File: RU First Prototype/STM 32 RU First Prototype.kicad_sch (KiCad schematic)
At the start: 79 parts, among them J1 Conn_01x02, J10 Conn_01x02, J2 USB_C_Receptacle, J3 Conn_01x02, J4 Conn_01x04, J5 Screw_Terminal, J6 Screw_Terminal, J7 Screw_Terminal, J8 Screw_Terminal, J9 Screw_Terminal, Q1 NMOS, Q1 SISA96DN-T1, Q2 SISA96DN-T1, Q3 SISA96DN-T1, Q4 SISA96DN-T1, SW1 SW_SPDT, U1 STM32F412RGTx, U2 AMS1117-3.3, U3 MS5611, U4 KX134-1211, U5 W25Q16JVSS, U6 TCAN330, U7 TCAN330, Y1 Crystal_25Mhz

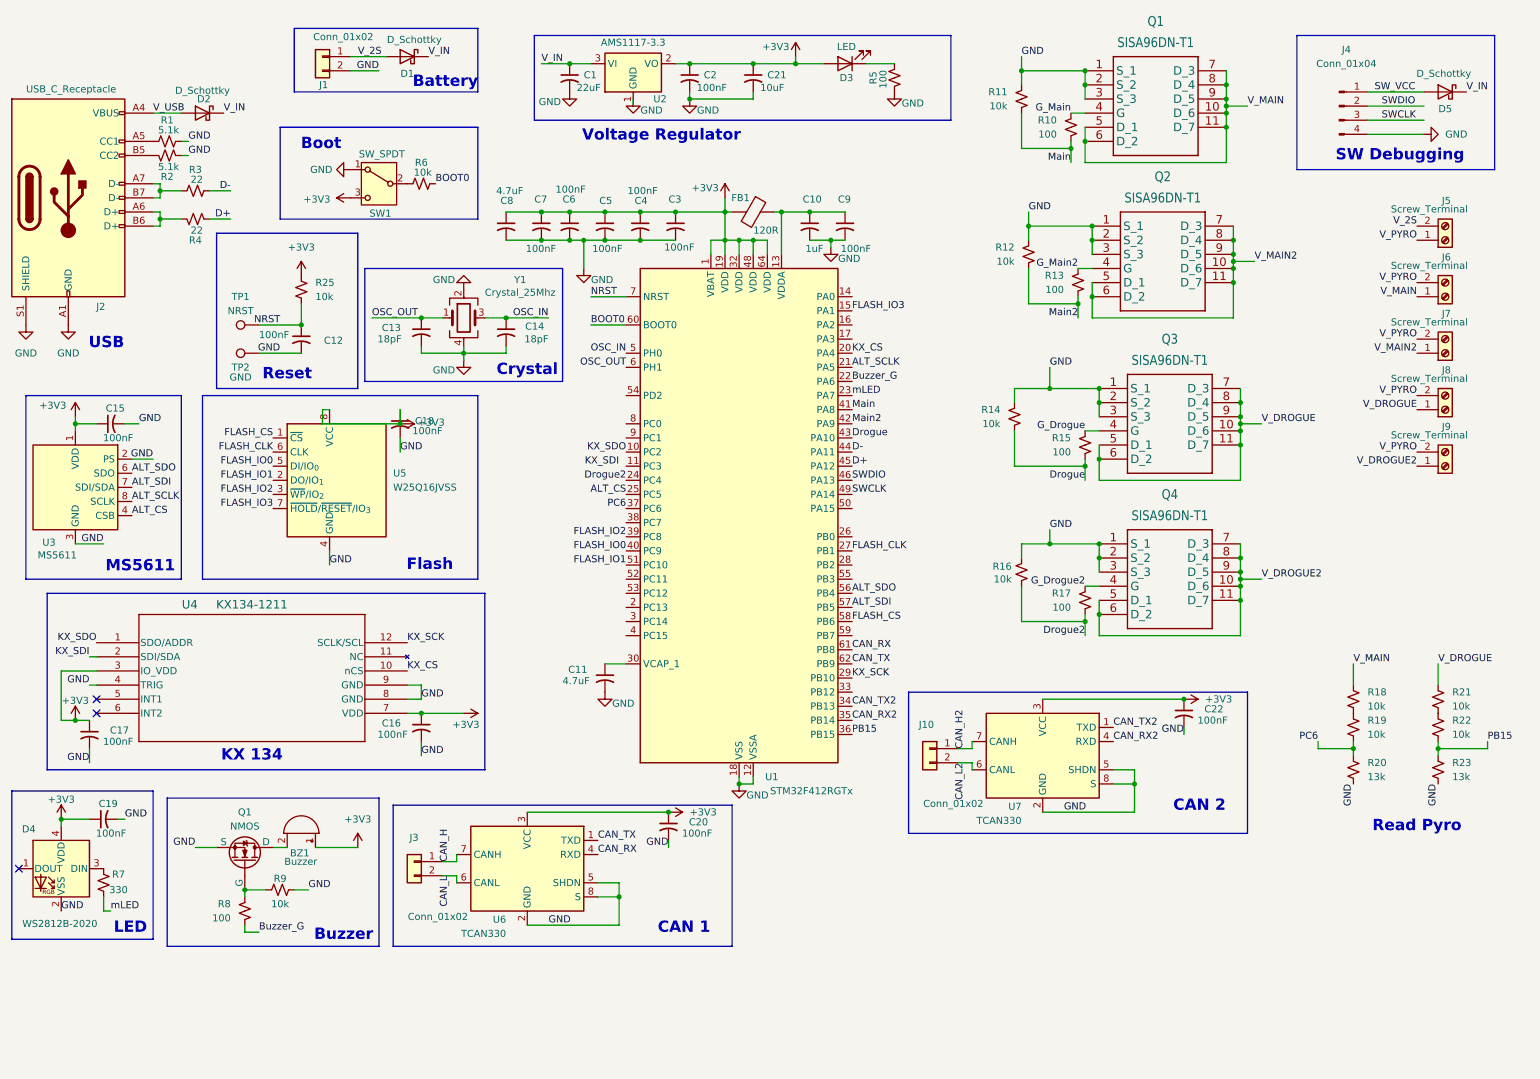
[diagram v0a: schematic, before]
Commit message: Schematic adjusted for symbols and footprint assignments, and I2C replaced with SPI
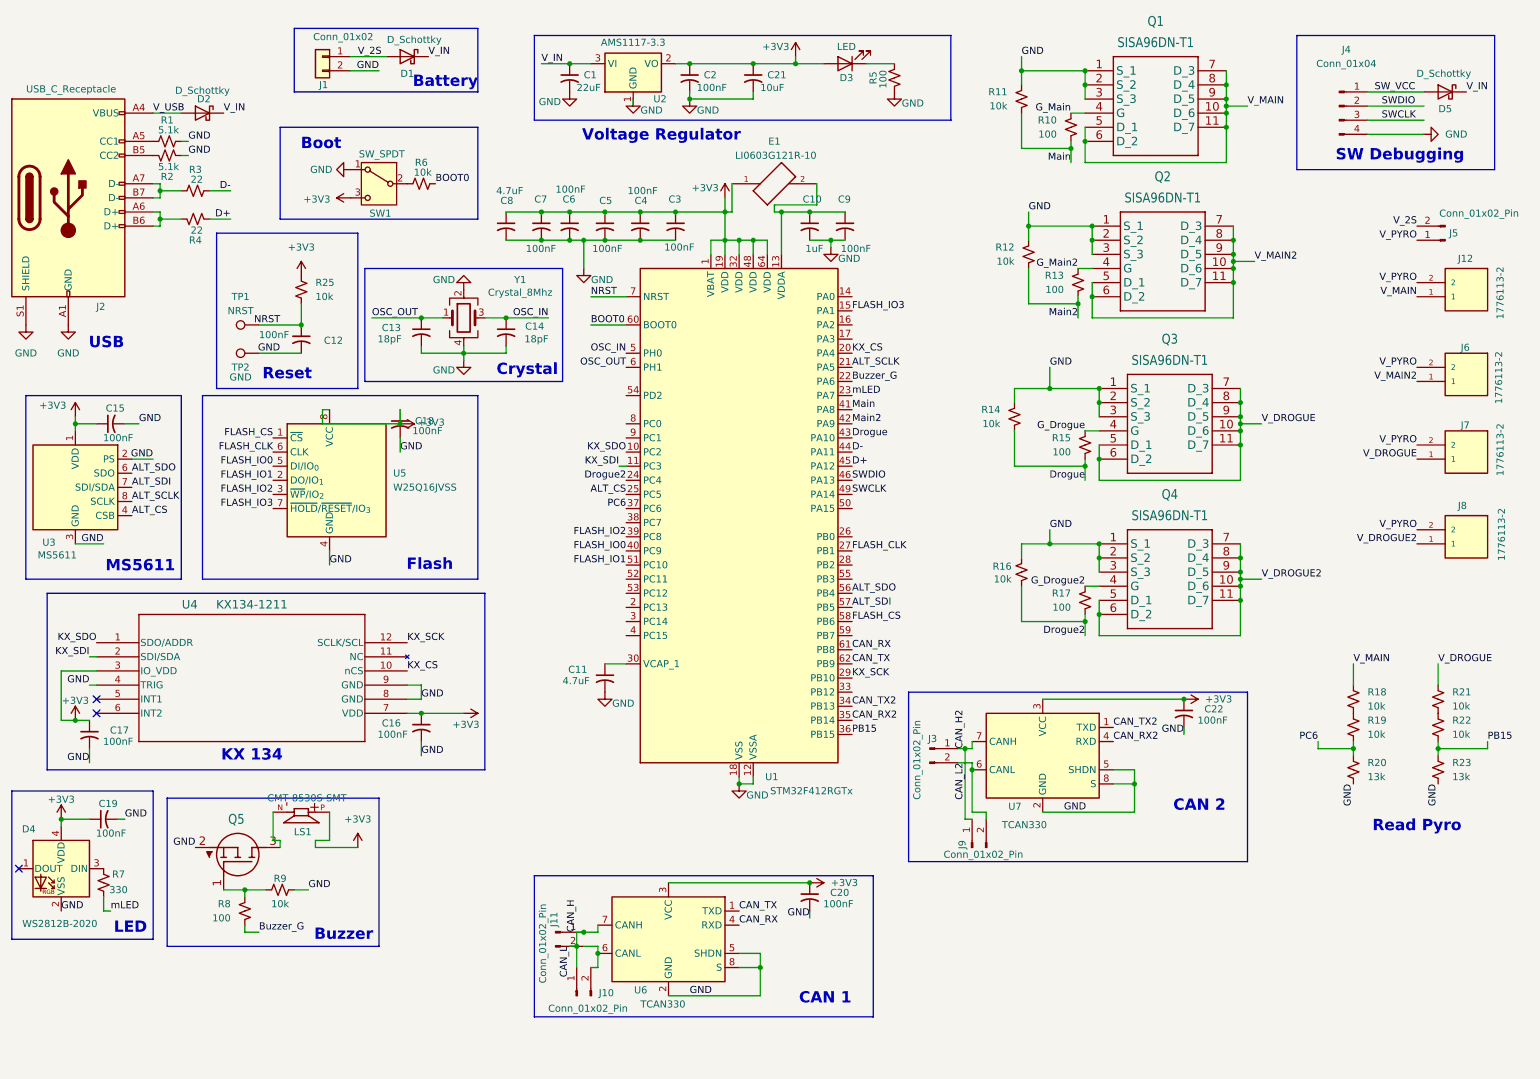
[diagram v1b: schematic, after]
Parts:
- removed BZ1: Buzzer, symbol Device:Buzzer
- removed FB1: 120R, symbol Device:FerriteBead
- removed J10, J3: Conn_01x02, Connector_AMASS:AMASS_XT30PW-F_1x02_P2.50mm_Horizontal, symbol Connector_Generic:Conn_01x02
- removed J5, J6, J7, J8, J9: Screw_Terminal, symbol Connector:Screw_Terminal_01x02
- removed Q1: NMOS, symbol Simulation_SPICE:NMOS
- added E1: LI0603G121R-10, LI0603G121R-10:FB_LI0603G121R-10, symbol LI0603G121R-10:LI0603G121R-10
- added J10, J11, J3, J5, J9: Conn_01x02_Pin, Connector_AMASS:AMASS_XT30PW-M_1x02_P2.50mm_Horizontal, symbol Connector:Conn_01x02_Pin
- added J12, J6, J7, J8: 1776113-2, 1776113-2:TE_1776113-2, symbol 1776113-2:1776113-2
- added LS1: CMT-8530S-SMT, CMT-8530S-SMT:CUI_CMT-8530S-SMT, symbol CMT-8530S-SMT:CMT-8530S-SMT
- added Q5: ~, CJ3400:SOT95P240X115-3N, symbol CJ3400:CJ3400
- Y1: value Crystal_25Mhz -> Crystal_8Mhz
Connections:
- net CAN_L2 is gone; now on net CAN_H2: U7.6 (CANL)
- net +3V3: now also E1.1, LS1.P
- net CAN_H: now also J10.1 (Pin_1), J11.1 (Pin_1)
- net CAN_H2: now also J3.1 (Pin_1), J3.2 (Pin_2), J9.1 (Pin_1), J9.2 (Pin_2)
- net GND: now also Q5.2 (S)
- net KX_SDI: now also U1.11 (PC3)
- net V_2S: now also J5.2 (Pin_2)
- net V_DROGUE: now also J7.1
- net V_DROGUE2: now also J8.1
- net V_MAIN: now also J12.1
- net V_MAIN2: now also J6.1
- net V_PYRO: now also J12.2, J5.1 (Pin_1), J6.2, J7.2, J8.2
- net at R8.1, R9.2: now also Q5.1 (G)
- net at C10.1, C9.1, U1.13 (VDDA): now also E1.2
- net CAN_L: no longer names the net of U6.6 (CANL)
- net CAN_L: now also J10.2 (Pin_2), J11.2 (Pin_2)
- new net: LS1.N, Q5.3 (D)
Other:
- moved on the sheet: C20, U6

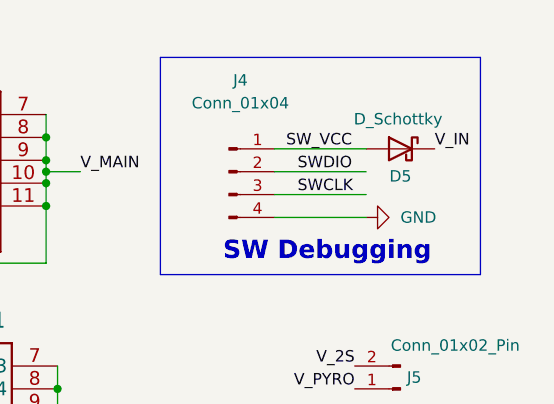
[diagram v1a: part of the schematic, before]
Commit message: Added missing footprints
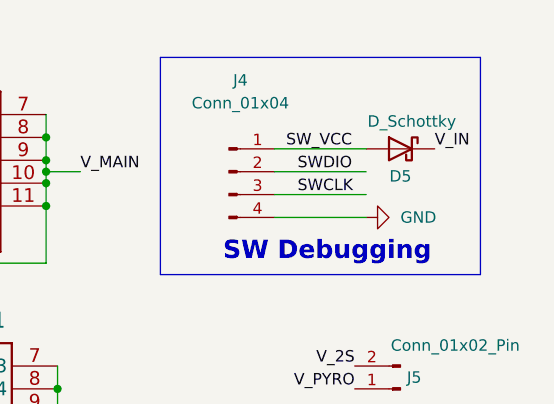
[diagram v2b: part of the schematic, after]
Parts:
- D1, D2, D5: footprint (none) -> Diode_SMD:D_SOD-128
- D3: footprint (none) -> Diode_SMD:D_0603_1608Metric
- Q1, Q2, Q3, Q4: footprint SISA96DN-T1-GE3:SIS862DNT1GE3 -> SISA96DN-T1:SIS862DNT1GE3
- U4: footprint LGA12_2X2X0P9_ROM -> KX134-1211:XDCR_KX003-1077
- Y1: footprint (none) -> Crystal:Crystal_SMD_7050-4Pin_7.0x5.0mm
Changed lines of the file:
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@@
 			)
 		)
-		(property "Footprint" "SISA96DN-T1-GE3:SIS862DNT1GE3"
+		(property "Footprint" "SISA96DN-T1:SIS862DNT1GE3"
 			(at 208.28 50.8 0)
 			(effects
@@
 			)
 		)
-		(property "Footprint" "SISA96DN-T1-GE3:SIS862DNT1GE3"
+		(property "Footprint" "SISA96DN-T1:SIS862DNT1GE3"
 			(at 209.55 80.01 0)
 			(effects
@@
 	)
 	(symbol
+		(lib_id "Device:D_Schottky")
+		(at 271.78 26.67 0)
+		(mirror y)
+		(unit 1)
+		(exclude_from_sim no)
+		(in_bom yes)
+		(on_board yes)
+		(dnp no)
+		(property "Reference" "D5"
+			(at 271.78 29.718 0)
+			(effects
+				(font
+					(size 1.27 1.27)
+				)
+			)
+		)
+		(property "Value" "D_Schottky"
+			(at 273.05 23.622 0)
+			(effects
+				(font
+					(size 1.27 1.27)
+				)
+			)
+		)
+		(property "Footprint" "Diode_SMD:D_SOD-128"
+			(at 271.78 26.67 0)
+			(effects
+				(font
+					(size 1.27 1.27)
+				)
+				(hide yes)
+			)
+		)
+		(property "Datasheet" "~"
+			(at 271.78 26.67 0)
+			(effects
+				(font
+					(size 1.27 1.27)
+				)
+				(hide yes)
+			)
+		)
+		(property "Description" "Schottky diode"
+			(at 271.78 26.67 0)
+			(effects
+				(font
+					(size 1.27 1.27)
+				)
+				(hide yes)
+			)
+		)
+		(pin "2"
+		)
+		(pin "1"
+		)
+		(instances
+			(project "STM 32 RU First Prototype"
+				(path "/73d1f315-8edb-4411-831f-b26c874dd7b7"
+					(reference "D5")
+					(unit 1)
+				)
+			)
+		)
+	)
+	(symbol
 		(lib_id "Device:C_Small_US")
 		(at 109.22 50.8 0)
@@
 			)
 		)
-		(property "Footprint" ""
+		(property "Footprint" "Diode_SMD:D_0603_1608Metric"
 			(at 163.83 21.59 0)
 			(effects
@@
 	)
 	(symbol
-		(lib_id "Device:D_Schottky")
-		(at 271.78 26.67 0)
-		(mirror y)
-		(unit 1)
-		(exclude_from_sim no)
-		(in_bom yes)
-		(on_board yes)
-		(dnp no)
-		(property "Reference" "D5"
-			(at 271.78 29.718 0)
-			(effects
-				(font
-					(size 1.27 1.27)
-				)
-			)
-		)
-		(property "Value" "D_Schottky"
-			(at 271.526 23.368 0)
-			(effects
-				(font
-					(size 1.27 1.27)
-				)
-			)
-		)
-		(property "Footprint" ""
-			(at 271.78 26.67 0)
-			(effects
-				(font
-					(size 1.27 1.27)
-				)
-				(hide yes)
-			)
-		)
-		(property "Datasheet" ""
-			(at 271.78 26.67 0)
-			(effects
-				(font
-					(size 1.27 1.27)
-				)
-				(hide yes)
-			)
-		)
-		(property "Description" "Schottky diode"
-			(at 271.78 26.67 0)
-			(effects
-				(font
-					(size 1.27 1.27)
-				)
-				(hide yes)
-			)
-		)
-		(pin "2"
-		)
-		(pin "1"
-		)
-		(instances
-			(project "STM 32 RU First Prototype"
-				(path "/73d1f315-8edb-4411-831f-b26c874dd7b7"
-					(reference "D5")
-					(unit 1)
-				)
-			)
-		)
-	)
-	(symbol
 		(lib_id "Device:C_Small_US")
 		(at 30.48 157.48 90)
@@
 			)
 		)
-		(property "Footprint" "SISA96DN-T1-GE3:SIS862DNT1GE3"
+		(property "Footprint" "SISA96DN-T1:SIS862DNT1GE3"
 			(at 207.01 22.86 0)
 			(effects
@@
 			)
 		)
-		(property "Footprint" "SISA96DN-T1-GE3:SIS862DNT1GE3"
+		(property "Footprint" "SISA96DN-T1:SIS862DNT1GE3"
 			(at 209.55 107.95 0)
 			(effects
@@
 			)
 		)
-		(property "Footprint" ""
+		(property "Footprint" "Crystal:Crystal_SMD_7050-4Pin_7.0x5.0mm"
 			(at 95.25 67.31 0)
 			(effects
@@
 			)
 		)
-		(property "Footprint" ""
+		(property "Footprint" "Diode_SMD:D_SOD-128"
 			(at 85.09 20.32 0)
 			(effects
@@
 			)
 		)
-		(property "Datasheet" ""
+		(property "Datasheet" "~"
 			(at 85.09 20.32 0)
 			(effects
@@
 			)
 		)
-		(property "Footprint" "LGA12_2X2X0P9_ROM"
+		(property "Footprint" "KX134-1211:XDCR_KX003-1077"
 			(at 29.21 125.73 0)
 			(effects
@@
 			)
 		)
-		(property "Footprint" ""
+		(property "Footprint" "Diode_SMD:D_SOD-128"
 			(at 48.26 30.48 0)
 			(effects
@@
 			)
 		)
-		(property "Datasheet" ""
+		(property "Datasheet" "~"
 			(at 48.26 30.48 0)
 			(effects

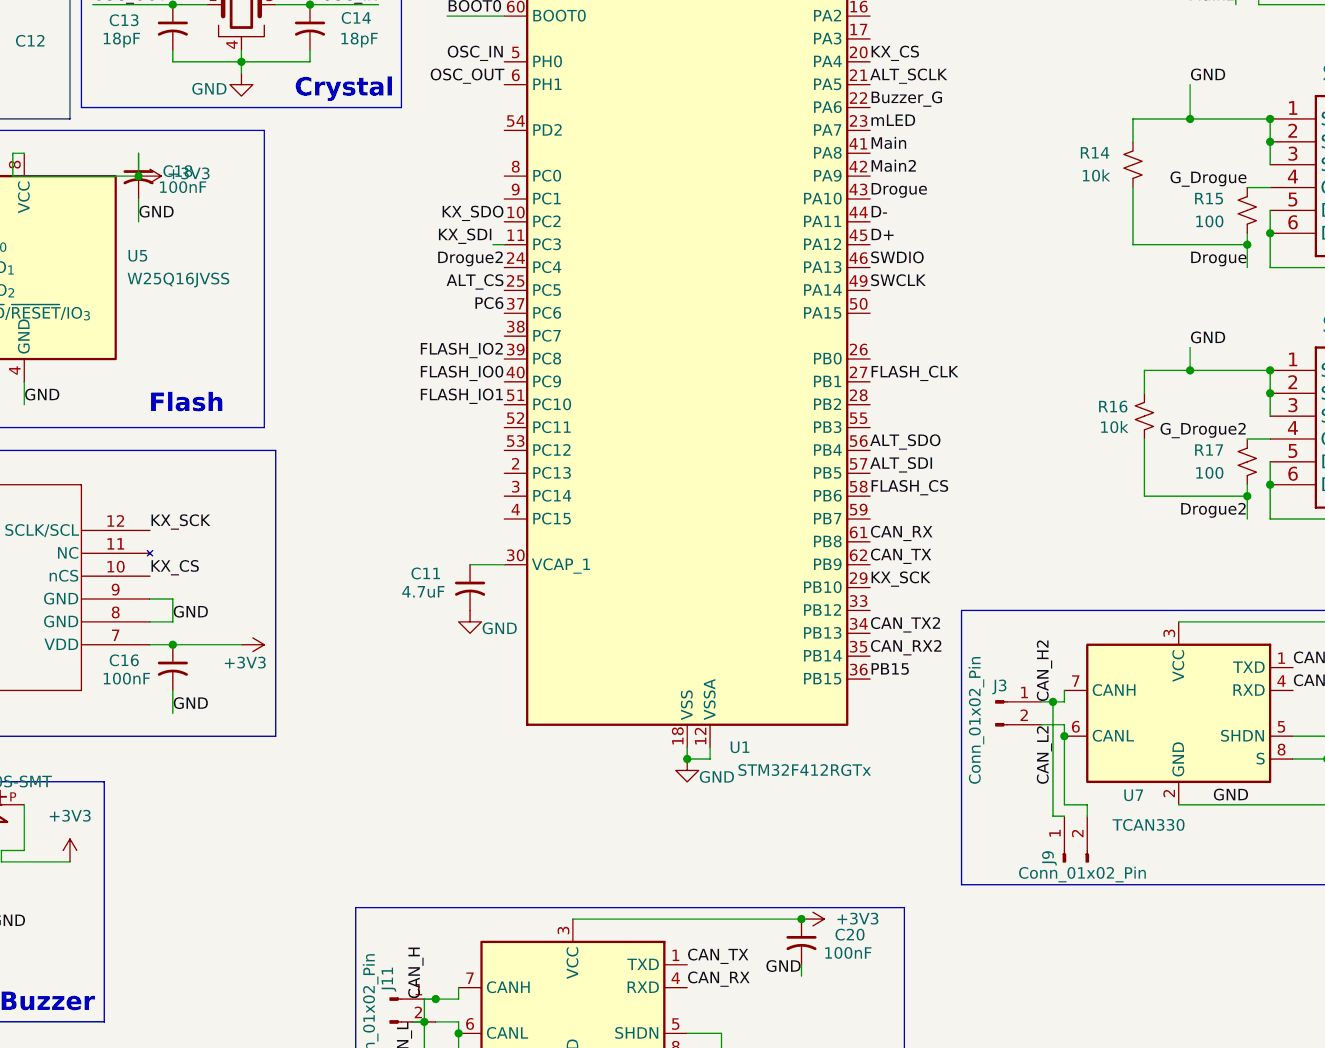
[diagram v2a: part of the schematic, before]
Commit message: Intermediate circuits of CAN, USB left, Spatial arrangement left
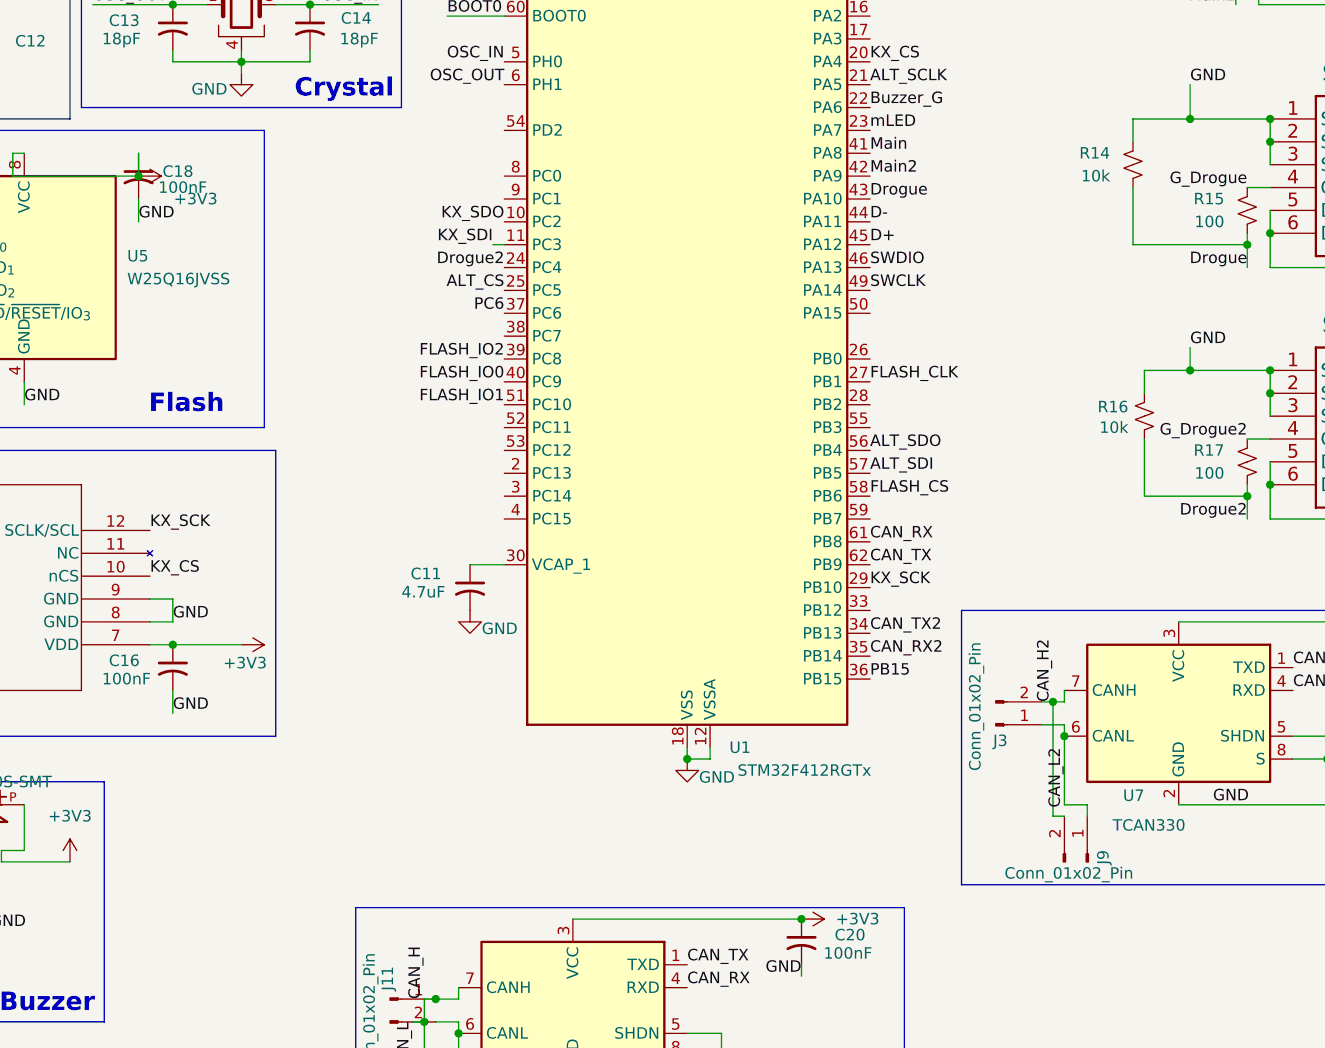
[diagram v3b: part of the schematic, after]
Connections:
- net CAN_H2: no longer J3.1 (Pin_1), J9.1 (Pin_1), U7.6 (CANL)
- new net CAN_L2: J3.1 (Pin_1), J9.1 (Pin_1), U7.6 (CANL)
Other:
- moved on the sheet: J9
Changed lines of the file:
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@@
 	(wire
 		(pts
-			(xy 184.15 147.32) (xy 186.69 147.32)
-		)
-		(stroke
-			(width 0)
-			(type default)
-		)
-	)
-	(wire
-		(pts
 			(xy 142.24 53.34) (xy 144.78 53.34)
 		)
@@
 	(wire
 		(pts
+			(xy 184.15 147.32) (xy 186.69 147.32)
+		)
+		(stroke
+			(width 0)
+			(type default)
+		)
+	)
+	(wire
+		(pts
 			(xy 40.64 50.8) (xy 39.37 50.8)
 		)
@@
 	(wire
 		(pts
-			(xy 185.42 144.78) (xy 185.42 157.48)
-		)
-		(stroke
-			(width 0)
-			(type default)
-		)
-	)
-	(wire
-		(pts
 			(xy 120.65 48.26) (xy 127 48.26)
 		)
@@
 	(wire
 		(pts
+			(xy 185.42 144.78) (xy 185.42 157.48)
+		)
+		(stroke
+			(width 0)
+			(type default)
+		)
+	)
+	(wire
+		(pts
 			(xy 68.58 162.56) (xy 76.2 162.56)
 		)
@@
 	)
 	(label "CAN_L2"
-		(at 185.42 147.32 270)
+		(at 186.69 149.86 270)
 		(effects
 			(font
@@
 		)
 		(property "Value" "+3V3"
-			(at 89.408 86.106 90)
+			(at 90.17 88.9 90)
 			(effects
 				(font
@@
 	(symbol
 		(lib_id "Connector:Conn_01x02_Pin")
-		(at 186.69 162.56 90)
+		(at 189.23 162.56 270)
+		(mirror x)
 		(unit 1)
 		(exclude_from_sim no)
@@
 		(dnp no)
 		(property "Reference" "J9"
-			(at 184.912 162.052 0)
+			(at 191.008 162.052 0)
 			(effects
 				(font
@@
 		)
 		(property "Value" "Conn_01x02_Pin"
-			(at 188.722 163.83 90)
+			(at 187.198 163.83 90)
 			(effects
 				(font
@@
 		)
 		(property "Footprint" "Connector_AMASS:AMASS_XT30PW-M_1x02_P2.50mm_Horizontal"
-			(at 186.69 162.56 0)
+			(at 189.23 162.56 0)
 			(effects
 				(font
@@
 		)
 		(property "Datasheet" "~"
-			(at 186.69 162.56 0)
+			(at 189.23 162.56 0)
 			(effects
 				(font
@@
 		)
 		(property "Description" "Generic connector, single row, 01x02, script generated"
-			(at 186.69 162.56 0)
+			(at 189.23 162.56 0)
 			(effects
 				(font
@@
 	(symbol
 		(lib_id "Connector:Conn_01x02_Pin")
-		(at 179.07 144.78 0)
+		(at 179.07 147.32 0)
+		(mirror x)
 		(unit 1)
 		(exclude_from_sim no)
@@
 		(dnp no)
 		(property "Reference" "J3"
-			(at 179.578 143.002 0)
+			(at 179.578 149.098 0)
 			(effects
 				(font
@@
 		)
 		(property "Value" "Conn_01x02_Pin"
-			(at 176.784 146.812 90)
+			(at 176.784 145.288 90)
 			(effects
 				(font
@@
 		)
 		(property "Footprint" "Connector_AMASS:AMASS_XT30PW-M_1x02_P2.50mm_Horizontal"
-			(at 179.07 144.78 0)
+			(at 179.07 147.32 0)
 			(effects
 				(font
@@
 		)
 		(property "Datasheet" "~"
-			(at 179.07 144.78 0)
+			(at 179.07 147.32 0)
 			(effects
 				(font
@@
 		)
 		(property "Description" "Generic connector, single row, 01x02, script generated"
-			(at 179.07 144.78 0)
+			(at 179.07 147.32 0)
 			(effects
 				(font
